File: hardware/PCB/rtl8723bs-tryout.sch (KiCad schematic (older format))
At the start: 13 parts

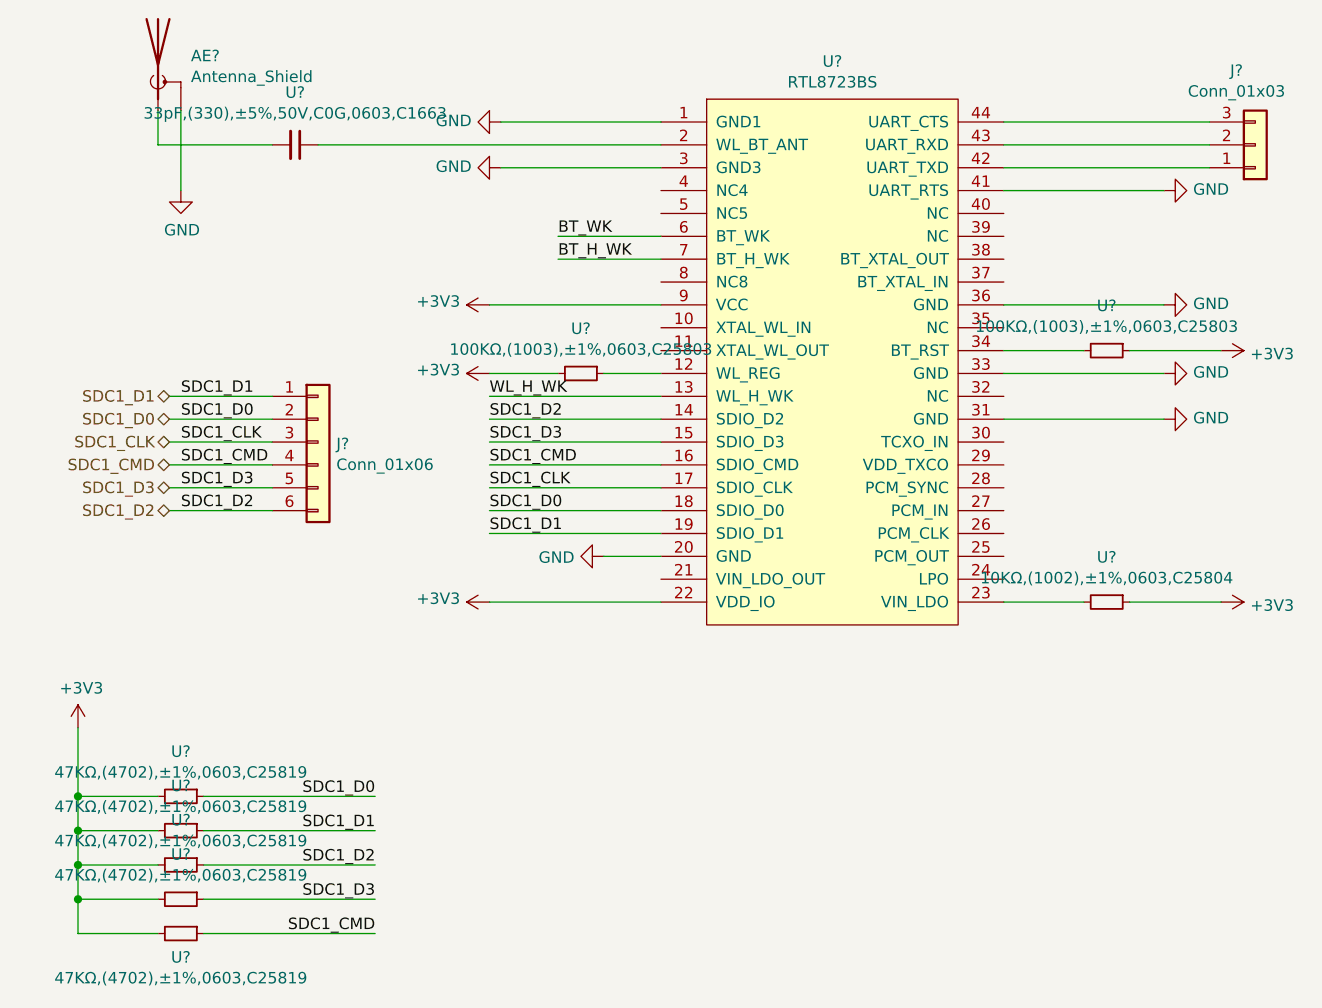
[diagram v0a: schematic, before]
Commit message: update rtl8723 circuit,
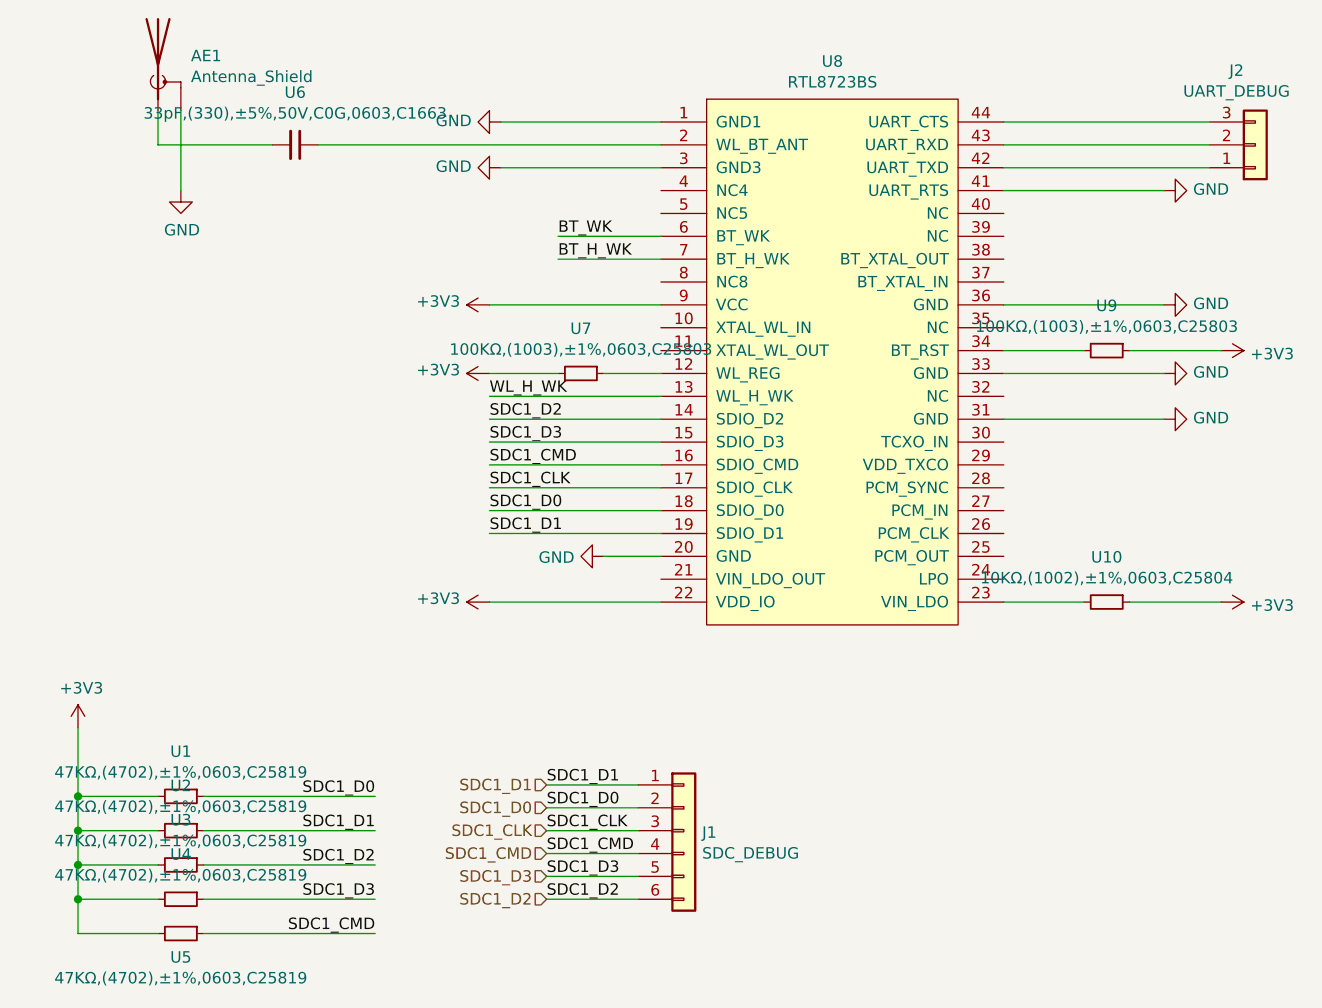
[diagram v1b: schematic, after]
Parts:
- AE1: renamed from AE?; footprint (none) -> footprint-lib:rainsun-AN9520
- J1: renamed from J?; value Conn_01x06 -> SDC_DEBUG; footprint (none) -> Connector_PinHeader_2.54mm:PinHeader_1x06_P2.54mm_Vertical
- J2: renamed from J?; value Conn_01x03 -> UART_DEBUG; footprint (none) -> Connector_PinHeader_2.54mm:PinHeader_1x03_P2.54mm_Vertical
- U8: renamed from U?; footprint (none) -> footprint-lib:RL-SM02BD(RTL8723BS)
- gave numbers to parts that had none: 9
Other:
- moved on the sheet: J1

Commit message: update,
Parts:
- renumbered J1 to J11, J2 to J12, U8 to U10, U9 to U11, U10 to U12, U1 to U3, U2 to U4, U3 to U5, U4 to U6, U5 to U7, U6 to U8, U7 to U9
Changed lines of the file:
@@
 $EndBitmap
 $Comp
-L taobao-components:RTL8723BS U8
+L taobao-components:RTL8723BS U10
 U 1 1 5E58D194
 P 4250 1950
-F 0 "U8" H 4200 3165 50  0000 C CNN
+F 0 "U10" H 4200 3165 50  0000 C CNN
 F 1 "RTL8723BS" H 4200 3074 50  0000 C CNN
 F 2 "footprint-lib:RL-SM02BD(RTL8723BS)" H 4250 1950 50  0001 C CNN
@@
 $EndComp
 $Comp
-L Connector_Generic:Conn_01x03 J2
+L Connector_Generic:Conn_01x03 J12
 U 1 1 5E58EF3B
 P 6050 1100
-F 0 "J2" H 5968 775 50  0000 C CNN
+F 0 "J12" H 5968 775 50  0000 C CNN
 F 1 "UART_DEBUG" H 5968 866 50  0000 C CNN
 F 2 "Connector_PinHeader_2.54mm:PinHeader_1x03_P2.54mm_Vertical" H 6050 1100 50  0001 C CNN
@@
 	4950 1200 5850 1200
 $Comp
-L power:GND #PWR09
+L power:GND #PWR034
 U 1 1 5E590680
 P 5650 1300
-F 0 "#PWR09" H 5650 1050 50  0001 C CNN
+F 0 "#PWR034" H 5650 1050 50  0001 C CNN
 F 1 "GND" V 5655 1172 50  0000 R CNN
 F 2 "" H 5650 1300 50  0001 C CNN
@@
 	5650 1300 4950 1300
 $Comp
-L power:GND #PWR010
+L power:GND #PWR035
 U 1 1 5E590CE9
 P 5650 1800
-F 0 "#PWR010" H 5650 1550 50  0001 C CNN
+F 0 "#PWR035" H 5650 1550 50  0001 C CNN
 F 1 "GND" V 5655 1672 50  0000 R CNN
 F 2 "" H 5650 1800 50  0001 C CNN
@@
 	5650 1800 4950 1800
 $Comp
-L power:GND #PWR011
+L power:GND #PWR036
 U 1 1 5E591FEA
 P 5650 2100
-F 0 "#PWR011" H 5650 1850 50  0001 C CNN
+F 0 "#PWR036" H 5650 1850 50  0001 C CNN
 F 1 "GND" V 5655 1972 50  0000 R CNN
 F 2 "" H 5650 2100 50  0001 C CNN
@@
 	5650 2100 4950 2100
 $Comp
-L power:GND #PWR012
+L power:GND #PWR037
 U 1 1 5E592859
 P 5650 2300
-F 0 "#PWR012" H 5650 2050 50  0001 C CNN
+F 0 "#PWR037" H 5650 2050 50  0001 C CNN
 F 1 "GND" V 5655 2172 50  0000 R CNN
 F 2 "" H 5650 2300 50  0001 C CNN
@@
 	5650 2300 4950 2300
 $Comp
-L customized_power:+3V3 #PWR014
+L customized_power:+3V3 #PWR039
 U 1 1 5E5934CE
 P 5900 3100
-F 0 "#PWR014" H 5900 2950 50  0001 C CNN
+F 0 "#PWR039" H 5900 2950 50  0001 C CNN
 F 1 "+3V3" V 5915 3228 50  0000 L CNN
 F 2 "" H 5900 3100 50  0001 C CNN
@@
 $EndComp
 $Comp
-L sz_jlc_resistor:10KΩ,(1002),±1%,0603,C25804 U10
+L sz_jlc_resistor:10KΩ,(1002),±1%,0603,C25804 U12
 U 1 1 5E5944D4
 P 5400 3100
-F 0 "U10" V 5204 3100 50  0000 C CNN
+F 0 "U12" V 5204 3100 50  0000 C CNN
 F 1 "10KΩ,(1002),±1%,0603,C25804" V 5295 3100 50  0000 C CNN
 F 2 "w_smd_resistors:r_0603" H 5400 2100 50  0001 C CNN
@@
 	5500 3100 5900 3100
 $Comp
-L customized_power:+3V3 #PWR013
+L customized_power:+3V3 #PWR038
 U 1 1 5E595D9D
 P 5900 2000
-F 0 "#PWR013" H 5900 1850 50  0001 C CNN
+F 0 "#PWR038" H 5900 1850 50  0001 C CNN
 F 1 "+3V3" V 5915 2128 50  0000 L CNN
 F 2 "" H 5900 2000 50  0001 C CNN
@@
 	5500 2000 5900 2000
 $Comp
-L Connector_Generic:Conn_01x06 J1
+L Connector_Generic:Conn_01x06 J11
 U 1 1 5E598990
 P 3550 4100
-F 0 "J1" H 3630 4092 50  0000 L CNN
+F 0 "J11" H 3630 4092 50  0000 L CNN
 F 1 "SDC_DEBUG" H 3630 4001 50  0000 L CNN
 F 2 "Connector_PinHeader_2.54mm:PinHeader_1x06_P2.54mm_Vertical" H 3550 4100 50  0001 C CNN
@@
 	2950 4400 3350 4400
 $Comp
-L sz_jlc_resistor:47KΩ,(4702),±1%,0603,C25819 U1
+L sz_jlc_resistor:47KΩ,(4702),±1%,0603,C25819 U3
 U 1 1 5E5A1C63
 P 1350 3950
-F 0 "U1" V 1154 3950 50  0000 C CNN
+F 0 "U3" V 1154 3950 50  0000 C CNN
 F 1 "47KΩ,(4702),±1%,0603,C25819" V 1245 3950 50  0000 C CNN
 F 2 "w_smd_resistors:r_0603" H 1350 2950 50  0001 C CNN
@@
 $EndComp
 $Comp
-L customized_power:+3V3 #PWR01
+L customized_power:+3V3 #PWR026
 U 1 1 5E5A285C
 P 900 3650
-F 0 "#PWR01" H 900 3500 50  0001 C CNN
+F 0 "#PWR026" H 900 3500 50  0001 C CNN
 F 1 "+3V3" H 915 3823 50  0000 C CNN
 F 2 "" H 900 3650 50  0001 C CNN
@@
 $EndComp
 $Comp
-L sz_jlc_resistor:47KΩ,(4702),±1%,0603,C25819 U2
+L sz_jlc_resistor:47KΩ,(4702),±1%,0603,C25819 U4
 U 1 1 5E5A2C30
 P 1350 4100
-F 0 "U2" V 1154 4100 50  0000 C CNN
+F 0 "U4" V 1154 4100 50  0000 C CNN
 F 1 "47KΩ,(4702),±1%,0603,C25819" V 1245 4100 50  0000 C CNN
 F 2 "w_smd_resistors:r_0603" H 1350 3100 50  0001 C CNN
@@
 $EndComp
 $Comp
-L sz_jlc_resistor:47KΩ,(4702),±1%,0603,C25819 U3
+L sz_jlc_resistor:47KΩ,(4702),±1%,0603,C25819 U5
 U 1 1 5E5A2DF7
 P 1350 4250
-F 0 "U3" V 1154 4250 50  0000 C CNN
+F 0 "U5" V 1154 4250 50  0000 C CNN
 F 1 "47KΩ,(4702),±1%,0603,C25819" V 1245 4250 50  0000 C CNN
 F 2 "w_smd_resistors:r_0603" H 1350 3250 50  0001 C CNN
@@
 $EndComp
 $Comp
-L sz_jlc_resistor:47KΩ,(4702),±1%,0603,C25819 U4
+L sz_jlc_resistor:47KΩ,(4702),±1%,0603,C25819 U6
 U 1 1 5E5A302E
 P 1350 4400
-F 0 "U4" V 1154 4400 50  0000 C CNN
+F 0 "U6" V 1154 4400 50  0000 C CNN
 F 1 "47KΩ,(4702),±1%,0603,C25819" V 1245 4400 50  0000 C CNN
 F 2 "w_smd_resistors:r_0603" H 1350 3400 50  0001 C CNN
@@
 $EndComp
 $Comp
-L sz_jlc_resistor:47KΩ,(4702),±1%,0603,C25819 U5
+L sz_jlc_resistor:47KΩ,(4702),±1%,0603,C25819 U7
 U 1 1 5E5A31FD
 P 1350 4550
-F 0 "U5" V 1454 4550 50  0000 C CNN
+F 0 "U7" V 1454 4550 50  0000 C CNN
 F 1 "47KΩ,(4702),±1%,0603,C25819" V 1545 4550 50  0000 C CNN
 F 2 "w_smd_resistors:r_0603" H 1350 3550 50  0001 C CNN
@@
 	2200 4550 1450 4550
 $Comp
-L power:GND #PWR06
+L power:GND #PWR031
 U 1 1 5E5AC216
 P 2750 1000
-F 0 "#PWR06" H 2750 750 50  0001 C CNN
+F 0 "#PWR031" H 2750 750 50  0001 C CNN
 F 1 "GND" V 2755 872 50  0000 R CNN
 F 2 "" H 2750 1000 50  0001 C CNN
@@
 	2750 1000 3450 1000
 $Comp
-L power:GND #PWR07
+L power:GND #PWR032
 U 1 1 5E5AF201
 P 2750 1200
-F 0 "#PWR07" H 2750 950 50  0001 C CNN
+F 0 "#PWR032" H 2750 950 50  0001 C CNN
 F 1 "GND" V 2755 1072 50  0000 R CNN
 F 2 "" H 2750 1200 50  0001 C CNN
@@
 BT_H_WK
 $Comp
-L sz_jlc_resistor:100KΩ,(1003),±1%,0603,C25803 U9
+L sz_jlc_resistor:100KΩ,(1003),±1%,0603,C25803 U11
 U 1 1 5E5B14A7
 P 5400 2000
-F 0 "U9" V 5204 2000 50  0000 C CNN
+F 0 "U11" V 5204 2000 50  0000 C CNN
 F 1 "100KΩ,(1003),±1%,0603,C25803" V 5295 2000 50  0000 C CNN
 F 2 "w_smd_resistors:r_0603" H 5400 1000 50  0001 C CNN
@@
 	3000 1600 3450 1600
 $Comp
-L customized_power:+3V3 #PWR03
+L customized_power:+3V3 #PWR028
 U 1 1 5E5B375D
 P 2700 1800
-F 0 "#PWR03" H 2700 1650 50  0001 C CNN
+F 0 "#PWR028" H 2700 1650 50  0001 C CNN
 F 1 "+3V3" V 2715 1928 50  0000 L CNN
 F 2 "" H 2700 1800 50  0001 C CNN
@@
 	3450 1800 2700 1800
 $Comp
-L customized_power:+3V3 #PWR04
+L customized_power:+3V3 #PWR029
 U 1 1 5E5B4D67
 P 2700 2100
-F 0 "#PWR04" H 2700 1950 50  0001 C CNN
+F 0 "#PWR029" H 2700 1950 50  0001 C CNN
 F 1 "+3V3" V 2715 2228 50  0000 L CNN
 F 2 "" H 2700 2100 50  0001 C CNN
@@
 $EndComp
 $Comp
-L sz_jlc_resistor:100KΩ,(1003),±1%,0603,C25803 U7
+L sz_jlc_resistor:100KΩ,(1003),±1%,0603,C25803 U9
 U 1 1 5E5B5081
 P 3100 2100
-F 0 "U7" V 2904 2100 50  0000 C CNN
+F 0 "U9" V 2904 2100 50  0000 C CNN
 F 1 "100KΩ,(1003),±1%,0603,C25803" V 2995 2100 50  0000 C CNN
 F 2 "w_smd_resistors:r_0603" H 3100 1100 50  0001 C CNN
@@
 	3200 2100 3450 2100
 $Comp
-L power:GND #PWR08
+L power:GND #PWR033
 U 1 1 5E5B8433
 P 3200 2900
-F 0 "#PWR08" H 3200 2650 50  0001 C CNN
+F 0 "#PWR033" H 3200 2650 50  0001 C CNN
 F 1 "GND" V 3205 2772 50  0000 R CNN
 F 2 "" H 3200 2900 50  0001 C CNN
@@
 	3200 2900 3450 2900
 $Comp
-L customized_power:+3V3 #PWR05
+L customized_power:+3V3 #PWR030
 U 1 1 5E5C0D12
 P 2700 3100
-F 0 "#PWR05" H 2700 2950 50  0001 C CNN
+F 0 "#PWR030" H 2700 2950 50  0001 C CNN
 F 1 "+3V3" V 2715 3228 50  0000 L CNN
 F 2 "" H 2700 3100 50  0001 C CNN
@@
 $EndComp
 $Comp
-L power:GND #PWR02
+L power:GND #PWR027
 U 1 1 5E5DE64D
 P 1350 1300
-F 0 "#PWR02" H 1350 1050 50  0001 C CNN
+F 0 "#PWR027" H 1350 1050 50  0001 C CNN
 F 1 "GND" H 1355 1127 50  0000 C CNN
 F 2 "" H 1350 1300 50  0001 C CNN
@@
 	1350 950  1350 1300
 $Comp
-L sz_jlc_capacitor:33pF,(330),±5%,50V,C0G,0603,C1663 U6
+L sz_jlc_capacitor:33pF,(330),±5%,50V,C0G,0603,C1663 U8
 U 1 1 5E5E0713
 P 1850 1100
-F 0 "U6" V 1621 1100 50  0000 C CNN
+F 0 "U8" V 1621 1100 50  0000 C CNN
 F 1 "33pF,(330),±5%,50V,C0G,0603,C1663" V 1712 1100 50  0000 C CNN
 F 2 "w_smd_cap:c_0603" H 1850 100 50  0001 C CNN
